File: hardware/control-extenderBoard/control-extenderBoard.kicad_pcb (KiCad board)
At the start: 4 copper layers, 197.5 x 135 mm, 150 parts, among them J1 12V + GND (TP), J10 SCL6 + GND (TP), J11 SDA6 + GND (TP), J12 3V3 + GND (TP), J13 12V + GND (TP), J14 SCL6 + GND (TP), J15 SDA6 + GND (TP), J16 12V + GND (TP), J17 24V IN, J18 GND, J19 3V3 + GND (TP), J2 12V Out, J20 SCL6 + GND (TP), J21 SDA6 + GND (TP), J22 SDA, SCL - ESP32, J23 I2C Reserve SCL/GND, J24 I2C Reserve SCL/GND, J25 I2C Reserve SDA/GND, J26 I2C Reserve SDA/GND, J27 CAT6-Shield, J28 CAT6-Shield, J29 Chassis, J3 5V out, J4 3V3 + GND (TP), J5 GND, J6 SCL7 Differential (TP), J7 SDA7 Differential (TP), J8 RS485, J9 3V3 out, P1 ISP, U1 MAX3485, U10 LM2576T-12, U13 AS5600_Breakout, U14 PCA9600D, U2 PCA9600D, U3 TCA9548A_1-to-8_I2C_Multiplex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, U4 LM2576T-3.3, U5 PCA9600D, U6 PCA82C251, U7 PCA82C251, U8 PCA9600D, U9 LM2576T-5

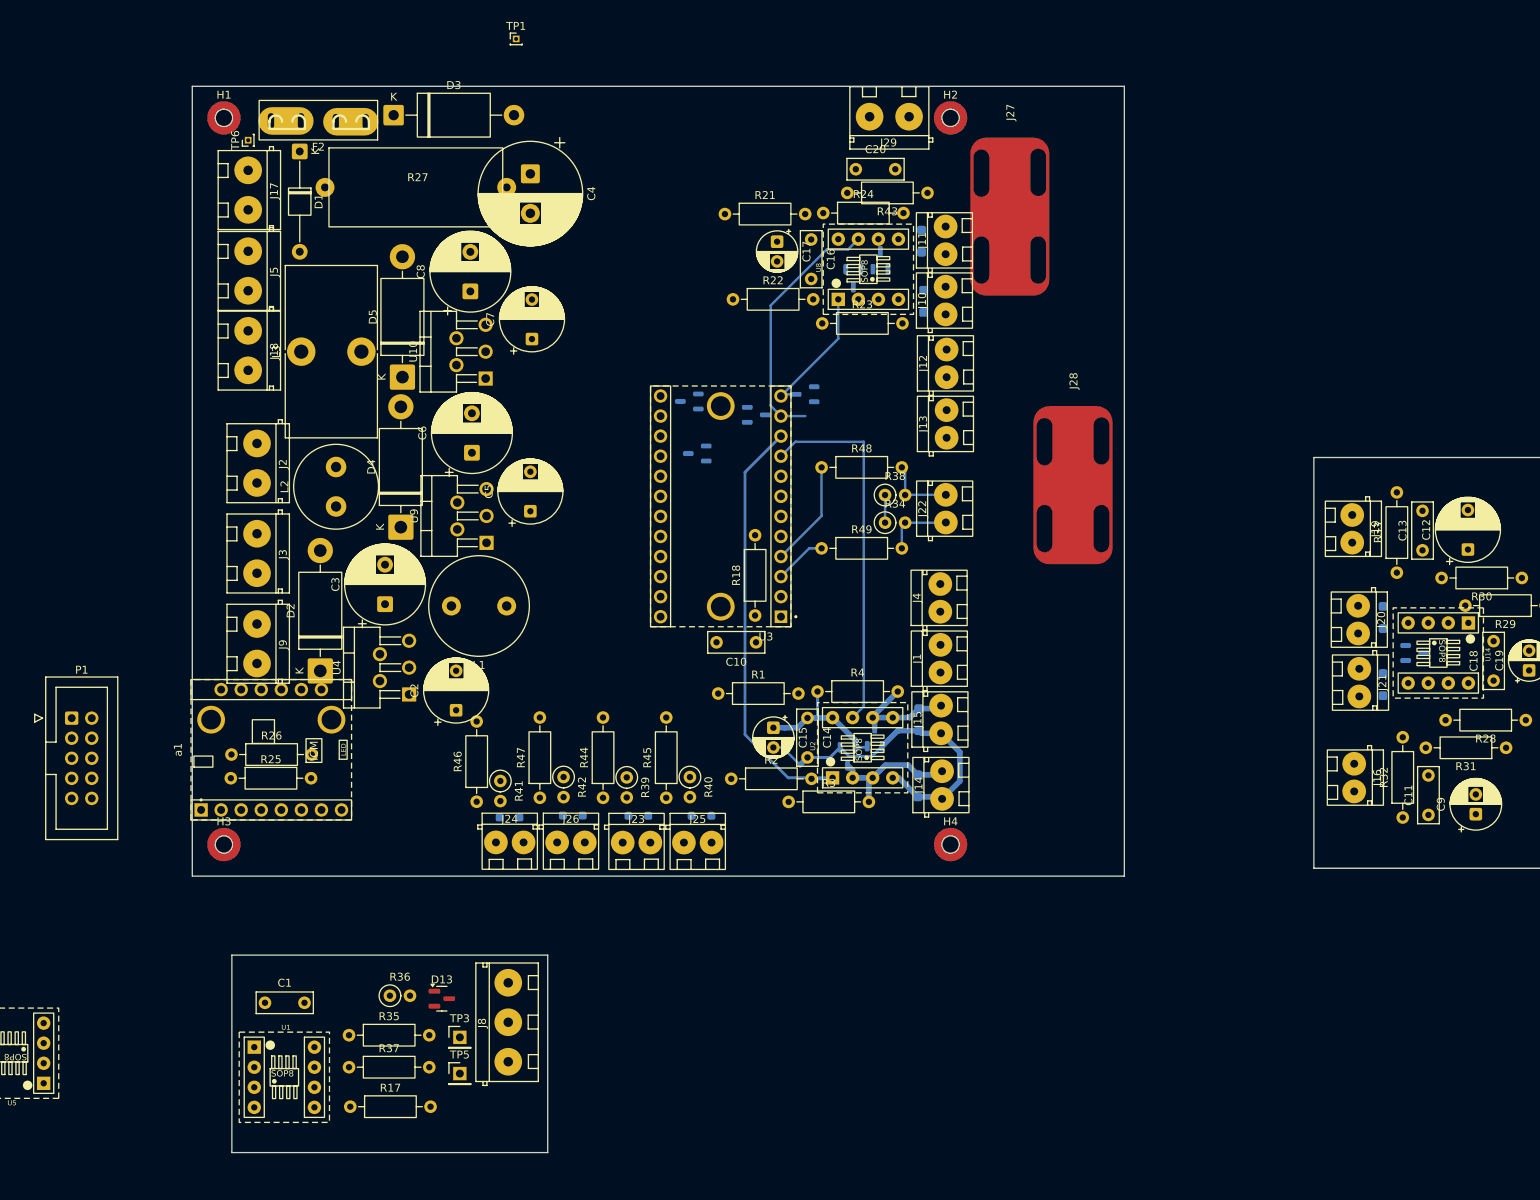
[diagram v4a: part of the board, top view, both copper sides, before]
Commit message: extenderBoard: Route supply + regulators
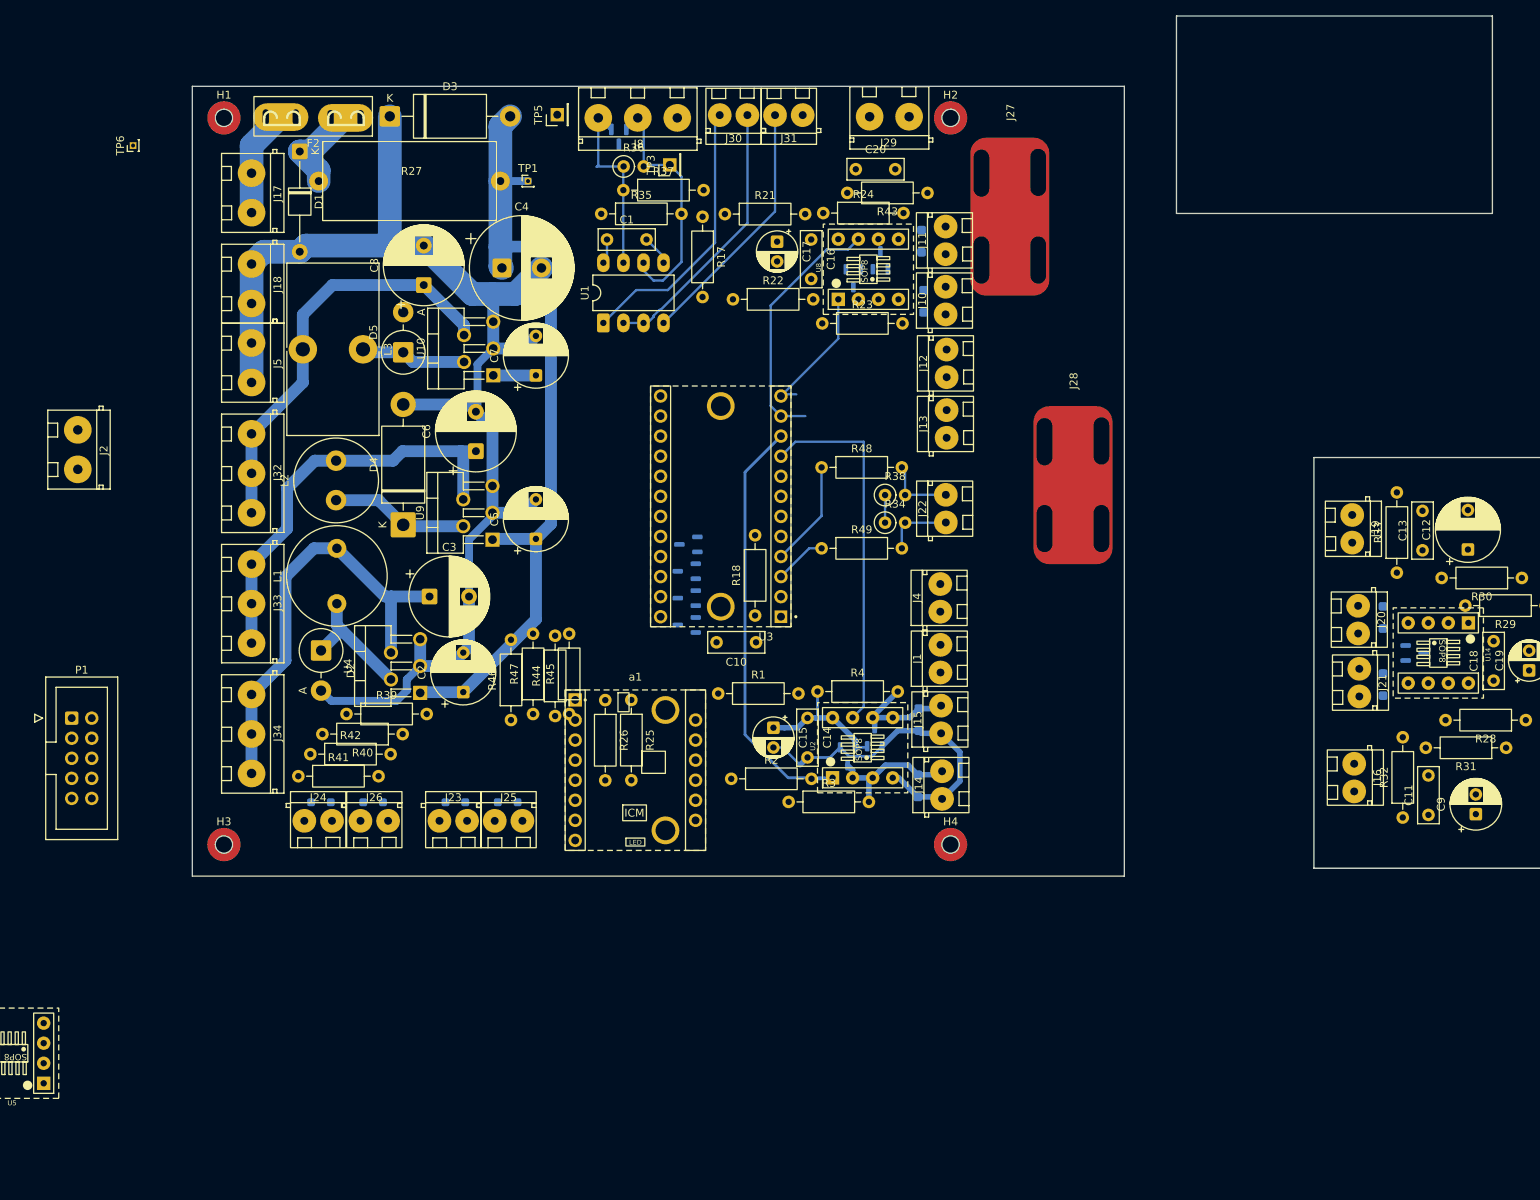
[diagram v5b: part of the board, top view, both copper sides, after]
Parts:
- removed J3: 5V out, terminals_libJonny:ScrewTerminal_P5mm_2Pin_FP10x8
- removed J9: 3V3 out, terminals_libJonny:ScrewTerminal_P5mm_2Pin_FP10x8
- added J30: RX TX, terminals_libJonny:ScrewTerminal_P3.5mm_2Pin_FP7x7, F.Cu at (115.3, 33.6)
- added J31: DIR, GND, terminals_libJonny:ScrewTerminal_P3.5mm_2Pin_FP7x7, F.Cu at (122.3, 33.6)
- added J32: 12V out, terminals_libJonny:ScrewTerminal_P5mm_3Pin_FP15x8, F.Cu at (52.5, 74.0)
- added J33: 5V out, terminals_libJonny:ScrewTerminal_P5mm_3Pin_FP15x8, F.Cu at (52.5, 90.5)
- added J34: 3V3 out, terminals_libJonny:ScrewTerminal_P5mm_3Pin_FP15x8, F.Cu at (52.5, 107.0)
- D13: moved to B.Cu
- D2, D5: footprint Diode_THT:D_DO-201AD_P15.24mm_Horizontal -> Diode_THT:D_DO-201AE_P5.08mm_Vertical_AnodeUp
- J2: value 12V Out -> GND
- R39, R40, R41, R42: footprint Resistor_THT:R_Axial_DIN0207_L6.3mm_D2.5mm_P2.54mm_Vertical -> Resistor_THT:R_Axial_DIN0207_L6.3mm_D2.5mm_P10.16mm_Horizontal
- U1: footprint modules_libJonny:Adapter-Board_SOP8_to_DIP8 -> Package_DIP:DIP-8_W7.62mm_LongPads
- moved TP5 122.0 mm to (91.2, 33.6), turned to 90 degrees
- moved J8 121.4 mm to (106.4, 34.0), turned to 180 degrees
- moved R17 121.2 mm to (109.6, 46.5), turned to -90 degrees
- moved R37 116.3 mm to (99.6, 43.1)
- moved TP3 113.6 mm to (105.5, 40.0), turned to 90 degrees
- moved D13 111.4 mm to (99.0, 36.4), turned to -90 degrees
- moved R36 109.1 mm to (99.6, 40.1)
- moved R35 108.8 mm to (96.8, 46.1)
- moved C1 105.9 mm to (97.5, 49.4)
- moved U1 103.7 mm to (97.0, 60.0), turned to 90 degrees
- moved R25 51.7 mm to (100.6, 107.7), turned to -90 degrees
- moved R26 47.8 mm to (97.3, 107.7), turned to -90 degrees
- moved a1 46.2 mm to (101.1, 116.6), turned to 0 degrees
- moved R40 36.8 mm to (71.6, 112.0), turned to 180 degrees
- moved R39 36.4 mm to (64.5, 109.5), turned to 0 degrees
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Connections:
- D19 pad 3: /I2C1_SDA -> /I2C7_SDA
- D23 pad 3: /I2C1_SCL -> /I2C7_SCL
- D24 pad 3: /I2C2_SDA -> /I2C6_SDA
- D25 pad 3: /I2C2_SCL -> /I2C6_SCL
- J2 pad 1: +12V -> GND
- J2 pad 2: +12V -> GND
- R25 pad 2: /I2C0_SCL -> /I2C5_SCL
- R26 pad 2: /I2C0_SDA -> /I2C5_SDA
- R44 pad 2: /I2C1_SCL -> /I2C7_SCL
- R45 pad 2: /I2C1_SDA -> /I2C7_SDA
- R46 pad 2: /I2C2_SCL -> /I2C6_SCL
- R47 pad 2: /I2C2_SDA -> /I2C6_SDA
- a1 pad 3: /I2C0_SCL -> /I2C5_SCL
- a1 pad 4: /I2C0_SDA -> /I2C5_SDA
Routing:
- net GND: track 42.6 -> 215.3 mm
- net +24V filtered: track 0.00 -> 108.1 mm
- net +3V3: track 3.50 -> 62.7 mm
- net +5V: track 0.00 -> 53.5 mm
- net +12V: track 18.0 -> 71.0 mm
- net /RS485_RX: track 0.00 -> 34.8 mm
- net /RS485_DIR: track 0.00 -> 34.7 mm
- net /RS485_TX: track 0.00 -> 32.2 mm
- net /RS485-A: track 0.00 -> 32.1 mm
- net /RS485-B: track 0.00 -> 24.2 mm
- net +BATT: track 0.00 -> 19.4 mm
- net Net-(D4-K): track 0.00 -> 17.5 mm
- net Net-(D2-K): track 0.00 -> 16.1 mm
- net Net-(D1-K): track 0.00 -> 14.2 mm
- net Net-(D5-K): track 0.00 -> 13.5 mm
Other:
- board size 197.5 x 135 mm -> 197.5 x 108.9 mm
- board text added: "BATT IN"

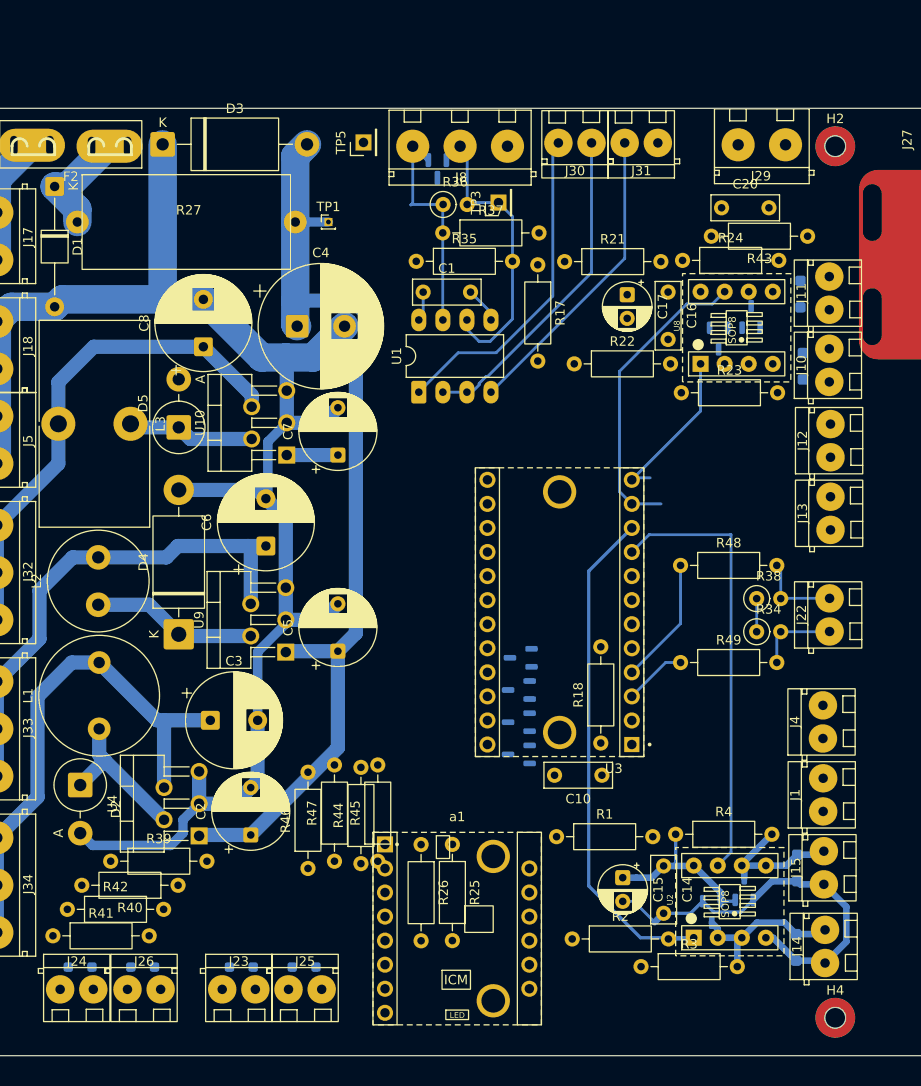
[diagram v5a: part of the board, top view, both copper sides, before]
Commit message: extenderBoard: Route I2C 12V boosting
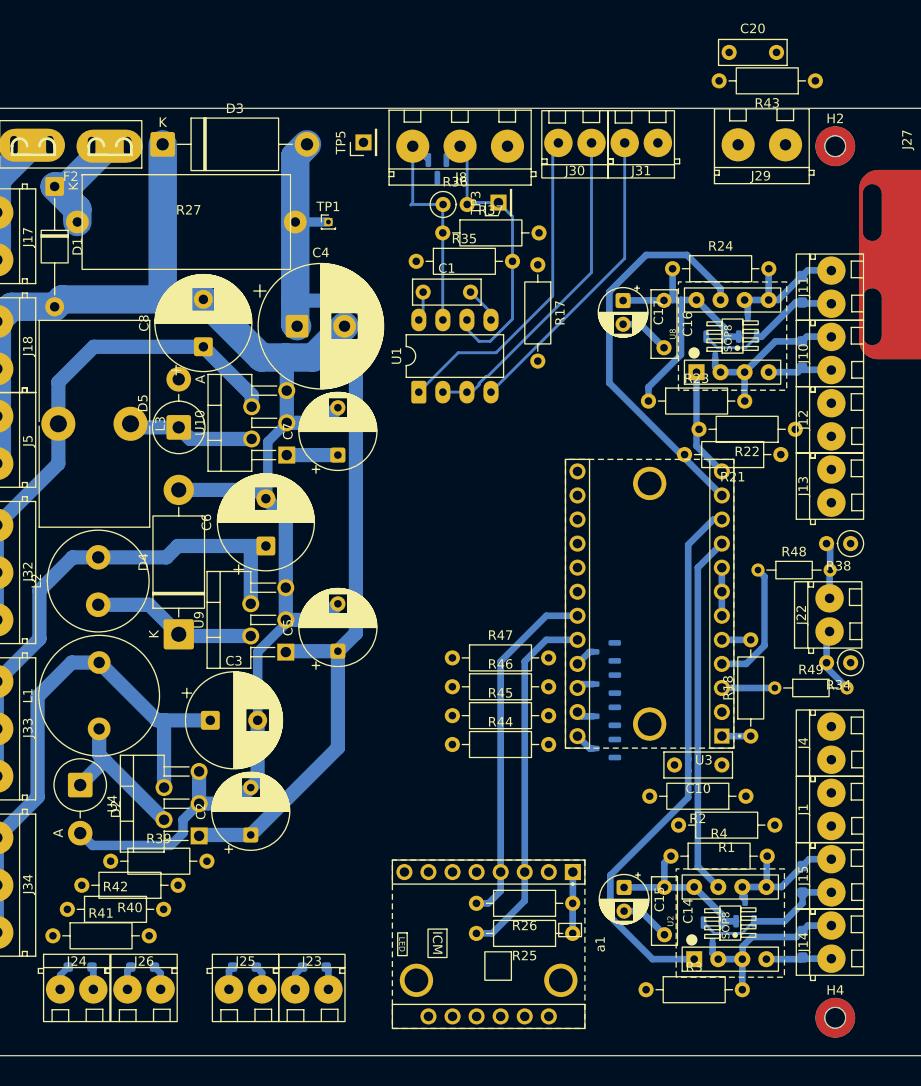
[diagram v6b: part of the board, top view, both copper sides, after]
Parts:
- R48, R49: footprint Resistor_THT:R_Axial_DIN0207_L6.3mm_D2.5mm_P10.16mm_Horizontal -> Resistor_THT:R_Axial_DIN0204_L3.6mm_D1.6mm_P7.62mm_Horizontal
- moved R21 30.6 mm to (135.3, 66.5), turned to 180 degrees
- moved R47 24.8 mm to (100.6, 88.0), turned to 0 degrees
- moved R46 24.5 mm to (100.6, 91.1), turned to 0 degrees
- moved R22 24.3 mm to (136.8, 63.9), turned to 180 degrees
- moved R2 23.7 mm to (131.6, 102.6), turned to 180 degrees
- moved R1 23.1 mm to (134.6, 105.7), turned to 180 degrees
- moved R45 17.3 mm to (100.6, 94.1), turned to 0 degrees
- moved R26 17.2 mm to (113.3, 113.9), turned to 180 degrees
- moved R43 16.4 mm to (138.9, 27.1)
- moved C20 16.4 mm to (129.8, 24.1)
- moved R44 15.9 mm to (100.6, 97.2), turned to 0 degrees
- moved R18 15.8 mm to (132.1, 96.3)
- moved R25 15.8 mm to (113.3, 117.1), turned to 180 degrees
- moved C10 12.7 mm to (129.0, 99.3)
- moved R38 11.5 mm to (142.6, 75.9), turned to 180 degrees
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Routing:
- net /I2C5_SCL: track 0.00 -> 38.3 mm
- net /I2C5_SDA: track 0.00 -> 37.5 mm
- net +12V: track 71.0 -> 100.4 mm
- net GND: track 215.3 -> 244.5 mm
- net /SCL_Boost2: track 0.00 -> 18.0 mm
- net /SDA_Boost2: track 0.00 -> 15.5 mm
- net /I2C1_SDA: track 32.2 -> 42.4 mm
- net /I2C0_SDA: track 46.7 -> 38.2 mm
- net +3V3: track 62.7 -> 68.7 mm
- net /I2C1_SCL: track 17.3 -> 11.6 mm
- net Net-(U3-RST): track 0.00 -> 3.05 mm
- net /ESP32_SCL: track 8.84 -> 5.96 mm
- net Net-(D17-A1): track 0.00 -> 2.70 mm
- net Net-(D18-A1): track 0.00 -> 2.67 mm
- net Net-(D6-A1): track 0.00 -> 2.51 mm
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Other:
- board text added: "All Isolated: - 5V, 3V3 - RS485 - 12x digital-in - 6x open drain - 2x relay - 2x 12V (P-MOS) - Buzzer - PWM (Servo signal)"
- board text added: "Gate V2.0 31.12.2024 pcb_isolated-gate-control"
